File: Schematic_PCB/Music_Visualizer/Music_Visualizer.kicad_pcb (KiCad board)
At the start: 2 copper layers, 141.5 x 82 mm, 232 parts, among them J3 Screw_Terminal_01x02, J5 Screw_Terminal_01x02, J6 3.5mm, Q1 DMP2123LQ-7, SW1 SW_Slide_DPDT, SW2 SW_SPST, U1 LM324, U10 LM3915N-1, U12 LM3915N-1, U13 LM3915N-1, U14 LM3915N-1, U15 LM3915N-1, U16 LM3915N-1, U3 LM324, U4 LM324, U5 LM324, U6 LM324, U7 LM324, U8 LM324

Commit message: pre RDC
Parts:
- removed TP10: T_pw, Custom_Footprints:TEST1Y
- removed TP11: T_mid, Custom_Footprints:TEST1Y
- removed TP12: T_ref, Custom_Footprints:TEST1Y
- removed TP13: T_grnd, Custom_Footprints:TEST1Y
- removed TP14: T_a_out, Custom_Footprints:TEST1Y
- removed TP8: T_a_in, Custom_Footprints:TEST1Y
- removed TP9: T_sig, Custom_Footprints:TEST1Y
- added C11: 100n, Custom_Footprints:custom_C_0805_2012Metric_Pad1.18x1.45mm_HandSolder, B.Cu at (35.5, 48.6)
- added C12: 100n, Custom_Footprints:custom_C_0805_2012Metric_Pad1.18x1.45mm_HandSolder, B.Cu at (35.5, 46.5)
- added C13: 100n, Custom_Footprints:custom_C_0805_2012Metric_Pad1.18x1.45mm_HandSolder, B.Cu at (34.8, 41.0)
- added C14: 100n, Custom_Footprints:custom_C_0805_2012Metric_Pad1.18x1.45mm_HandSolder, B.Cu at (34.8, 43.0)
- added C15: 100n, Custom_Footprints:custom_C_0805_2012Metric_Pad1.18x1.45mm_HandSolder, B.Cu at (27.0, 41.3)
- added C16: 100n, Custom_Footprints:custom_C_0805_2012Metric_Pad1.18x1.45mm_HandSolder, B.Cu at (27.0, 44.2)
- added C17: 10u, Custom_Footprints:custom_C_0805_2012Metric_Pad1.18x1.45mm_HandSolder, F.Cu at (26.2, 40.3)
- added C60: 100n, Custom_Footprints:custom_C_0805_2012Metric_Pad1.18x1.45mm_HandSolder, B.Cu at (30.7, 47.2)
- added D11: LED, PCM_SparkFun-LED:LED_1206_3216Metric_Green, F.Cu at (30.7, 37.1)
- added D12: LED, PCM_SparkFun-LED:LED_1206_3216Metric_Green, F.Cu at (30.7, 34.8)
- added D13: LED, PCM_SparkFun-LED:LED_1206_3216Metric_Green, F.Cu at (30.8, 32.5)
- added D14: LED, PCM_SparkFun-LED:LED_1206_3216Metric_Green, F.Cu at (30.7, 30.3)
- added D15: LED, PCM_SparkFun-LED:LED_1206_3216Metric_Green, F.Cu at (30.8, 28.0)
- added D16: LED, PCM_SparkFun-LED:LED_1206_3216Metric_Green, F.Cu at (30.8, 25.8)
- added D17: LED, PCM_SparkFun-LED:LED_1206_3216Metric_Green, F.Cu at (30.8, 23.5)
- added D18: LED, PCM_SparkFun-LED:LED_1206_3216Metric_Yellow, F.Cu at (30.8, 21.3)
- added D19: LED, PCM_SparkFun-LED:LED_1206_3216Metric_Yellow, F.Cu at (30.8, 19.0)
- added D20: LED, PCM_SparkFun-LED:LED_1206_3216Metric_Red, F.Cu at (30.8, 16.8)
- added R13: 27k, Custom_Footprints:R_0805_2012Metric_Pad1.20x1.40mm_HandSolder, F.Cu at (36.0, 47.6)
- added R14: 6.8k, Custom_Footprints:R_0805_2012Metric_Pad1.20x1.40mm_HandSolder, F.Cu at (30.8, 39.2)
- added R15: 120k, Custom_Footprints:R_0805_2012Metric_Pad1.20x1.40mm_HandSolder, B.Cu at (32.7, 47.3)
- added R16: 12k, Custom_Footprints:R_0805_2012Metric_Pad1.20x1.40mm_HandSolder, F.Cu at (35.2, 39.3)
- added R17: 3.3k, Custom_Footprints:R_0805_2012Metric_Pad1.20x1.40mm_HandSolder, F.Cu at (36.0, 43.5)
- added R18: 56k, Custom_Footprints:R_0805_2012Metric_Pad1.20x1.40mm_HandSolder, B.Cu at (32.0, 42.0)
- added R19: 18k, Custom_Footprints:R_0805_2012Metric_Pad1.20x1.40mm_HandSolder, B.Cu at (29.2, 39.3)
- added R20: 15k, Custom_Footprints:R_0805_2012Metric_Pad1.20x1.40mm_HandSolder, B.Cu at (27.0, 47.0)
- added R21: 39k, Custom_Footprints:R_0805_2012Metric_Pad1.20x1.40mm_HandSolder, B.Cu at (30.0, 42.0)
- added R22: 1k, Custom_Footprints:R_0805_2012Metric_Pad1.20x1.40mm_HandSolder, B.Cu at (29.2, 27.6)
- added R76: 680, Custom_Footprints:R_0805_2012Metric_Pad1.20x1.40mm_HandSolder, B.Cu at (29.2, 20.8)
- added TP2: T_B, Custom_Footprints:NEW_2_TestPoint_Loop_D2.60mm_Drill0.9mm_Beaded, B.Cu at (30.6, 13.8)
- added T_gnd1: T_gnd, Custom_Footprints:NEW_2_TestPoint_Loop_D2.60mm_Drill0.9mm_Beaded, F.Cu at (68.6, 58.8)
- added T_in1: T_in, Custom_Footprints:NEW_2_TestPoint_Loop_D2.60mm_Drill0.9mm_Beaded, F.Cu at (52.6, 52.3)
- added T_mid1: T_mid, Custom_Footprints:NEW_2_TestPoint_Loop_D2.60mm_Drill0.9mm_Beaded, F.Cu at (58.0, 52.8)
- added T_out1: T_out, Custom_Footprints:NEW_2_TestPoint_Loop_D2.60mm_Drill0.9mm_Beaded, F.Cu at (40.3, 52.3)
- added T_pw1: T_pw, Custom_Footprints:NEW_2_TestPoint_Loop_D2.60mm_Drill0.9mm_Beaded, F.Cu at (85.1, 60.6)
- added T_ref1: T_ref, Custom_Footprints:NEW_2_TestPoint_Loop_D2.60mm_Drill0.9mm_Beaded, F.Cu at (35.3, 53.1)
- added T_sig1: T_sig, Custom_Footprints:NEW_2_TestPoint_Loop_D2.60mm_Drill0.9mm_Beaded, F.Cu at (38.1, 52.3)
- added U11: LM3915N-1, Package_DIP:DIP-18_W7.62mm, B.Cu at (27.0, 36.9)
- added U2: LM324, Package_SO:SOIC-14_3.9x8.7mm_P1.27mm, F.Cu at (31.0, 44.8)
- C54, C58, C9, R11, R12: moved to F.Cu
- H1: footprint MountingHole:MountingHole_3.2mm_M3_DIN965 -> Custom_Footprints:Apgriezts_MountingHole_2.2mm_M2
- H2, H3, H4: footprint MountingHole:MountingHole_3.2mm_M3 -> Custom_Footprints:Apgriezts_MountingHole_2.2mm_M2
- J3, J5: footprint TerminalBlock_Phoenix:TerminalBlock_Phoenix_MPT-0,5-2-2.54_1x02_P2.54mm_Horizontal -> Connector_JST:JST_EH_B2B-EH-A_1x02_P2.50mm_Vertical
- J6: footprint PCM_SparkFun-Connector:ScrewTerminal_1x03_P3.5mm_Horizontal_Black -> Connector_JST:JST_EH_B2B-EH-A_1x02_P2.50mm_Vertical
- Q1: moved to B.Cu
- TP1, TP3, TP4, TP5, TP6, TP7: footprint Custom_Footprints:TEST1Y -> Custom_Footprints:NEW_2_TestPoint_Loop_D2.60mm_Drill0.9mm_Beaded; moved to B.Cu
- moved H3 134.5 mm to (36.1, 58.1)
- moved H4 112.2 mm to (57.1, 58.1)
- moved C57 99.3 mm to (32.1, 55.9), turned to -90 degrees
- moved C56 92.5 mm to (25.5, 56.1), turned to 0 degrees
- moved RV2 90.7 mm to (25.1, 53.1)
- moved R74 88.0 mm to (29.3, 56.1), turned to 180 degrees
- moved RV1 84.1 mm to (15.3, 53.1), turned to 0 degrees
- moved C54 50.4 mm to (63.2, 54.8), turned to 180 degrees
- moved C58 50.1 mm to (88.7, 58.8)
- moved R82 49.0 mm to (88.9, 53.3), turned to 90 degrees
- moved SW1 48.8 mm to (48.5, 54.0), turned to -90 degrees
- moved SW2 48.2 mm to (95.2, 53.2), turned to 0 degrees
- moved D71 48.1 mm to (86.8, 53.3), turned to 90 degrees
- moved Q1 45.2 mm to (87.8, 53.6), turned to -90 degrees
- moved J6 42.9 mm to (96.5, 56.1)
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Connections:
- J6 pad 1: Net-(J6-Pin_1) -> GND
- J6 pad 2: GND -> Net-(J6-+)
- Q1 pad 1: Net-(J6-Pin_1) -> Net-(J6-+)
- RV1 pad 1: GND -> unconnected-(RV1-Pad1)
- RV1 pad 3: unconnected-(RV1-Pad3) -> GND
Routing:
- net LED_Brightness_Control: track 292.2 -> 136.3 mm
- net VCC4_5: track 210.8 -> 320.3 mm, vias 7 -> 9
- net +9V: track 300.3 -> 408.0 mm, vias 7 -> 9
- net Vsig: track 56.8 -> 128.4 mm, vias 0 -> 2
- net Net-(C8-Pad2): track 0.00 -> 49.1 mm, vias 0 -> 1
- net Rhi_Value: track 182.1 -> 141.6 mm
- net VBass: track 0.00 -> 33.3 mm, vias 0 -> 1
- net Net-(U8D-+): track 0.00 -> 25.5 mm, vias 0 -> 1
- net Net-(C9-Pad1): track 0.00 -> 15.2 mm
- net Net-(C11-Pad1): track 0.00 -> 14.7 mm, vias 0 -> 2
- net Net-(Q1-S): track 0.00 -> 14.4 mm
- net Net-(J6-+): track 0.00 -> 13.4 mm
- net Net-(C11-Pad2): track 0.00 -> 12.0 mm, vias 0 -> 2
- net Right jack: track 0.00 -> 11.3 mm
- net Net-(U8B-+): track 0.00 -> 10.5 mm
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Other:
- board size 141.5 x 82 mm -> 88.2 x 50.2 mm
- board text added: "+9v"
- board text added: "-24-"
- board text added: "-45-"
- board text added: "-46-"
- board text added: "<IN OUT>"
- board text added: "<OUT IN>"
- board text added: "Brightness"
- board text added: "Mode"
- board text added: "ON OFF"
- board text added: "Sensitivity"
- board text removed: "Bass[60Hz:150Hz]"
- board text removed: "Brilliance[6kHz:20kHz]"
- board text removed: "LED Brightness"
- board text removed: "Low Midrange[150Hz:400Hz]"
- board text removed: "Midrange[400Hz:1kHz]"
- board text removed: "Presence[2.5kHz:6kHz]"
- board text removed: "Upper-Midrange[1kHz:2.5kHz]"
- board text removed: "Volume Range"

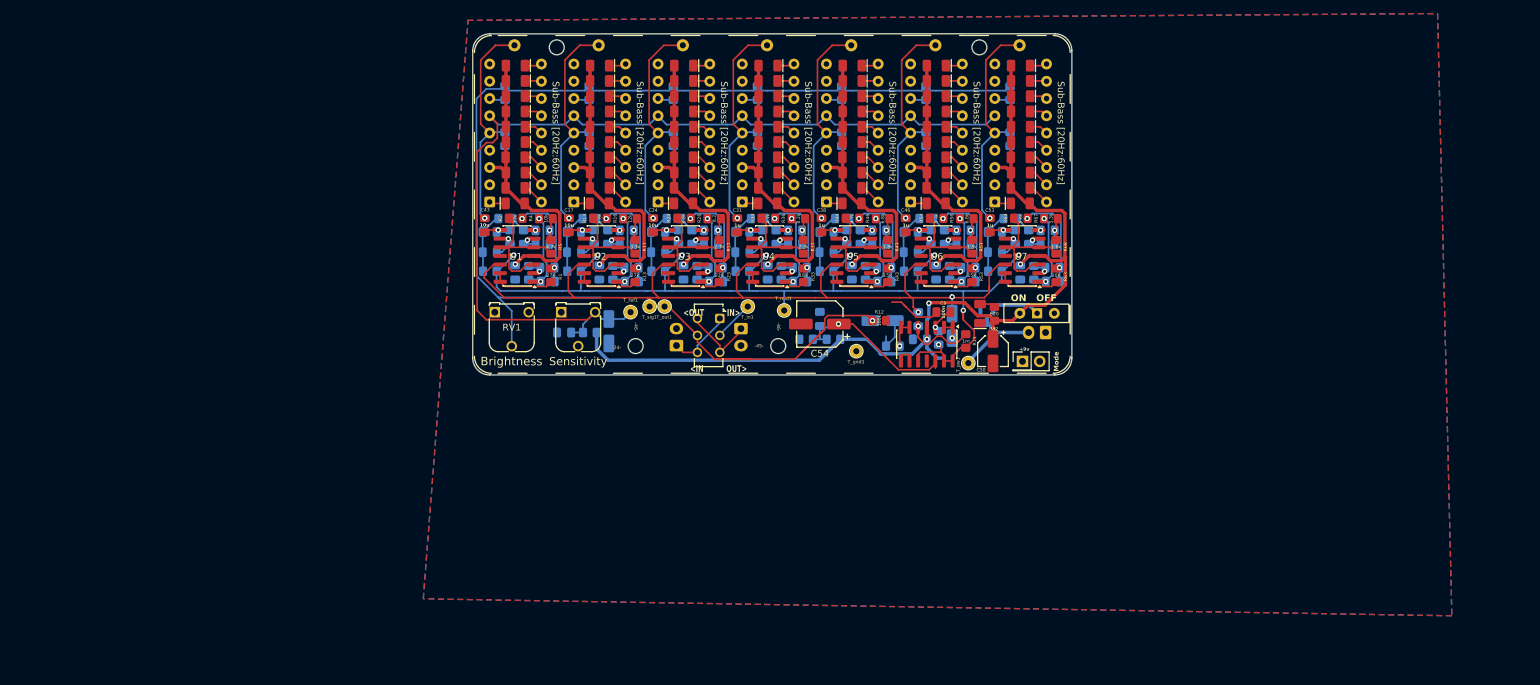
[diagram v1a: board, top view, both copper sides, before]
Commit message: Fixed DRC erros
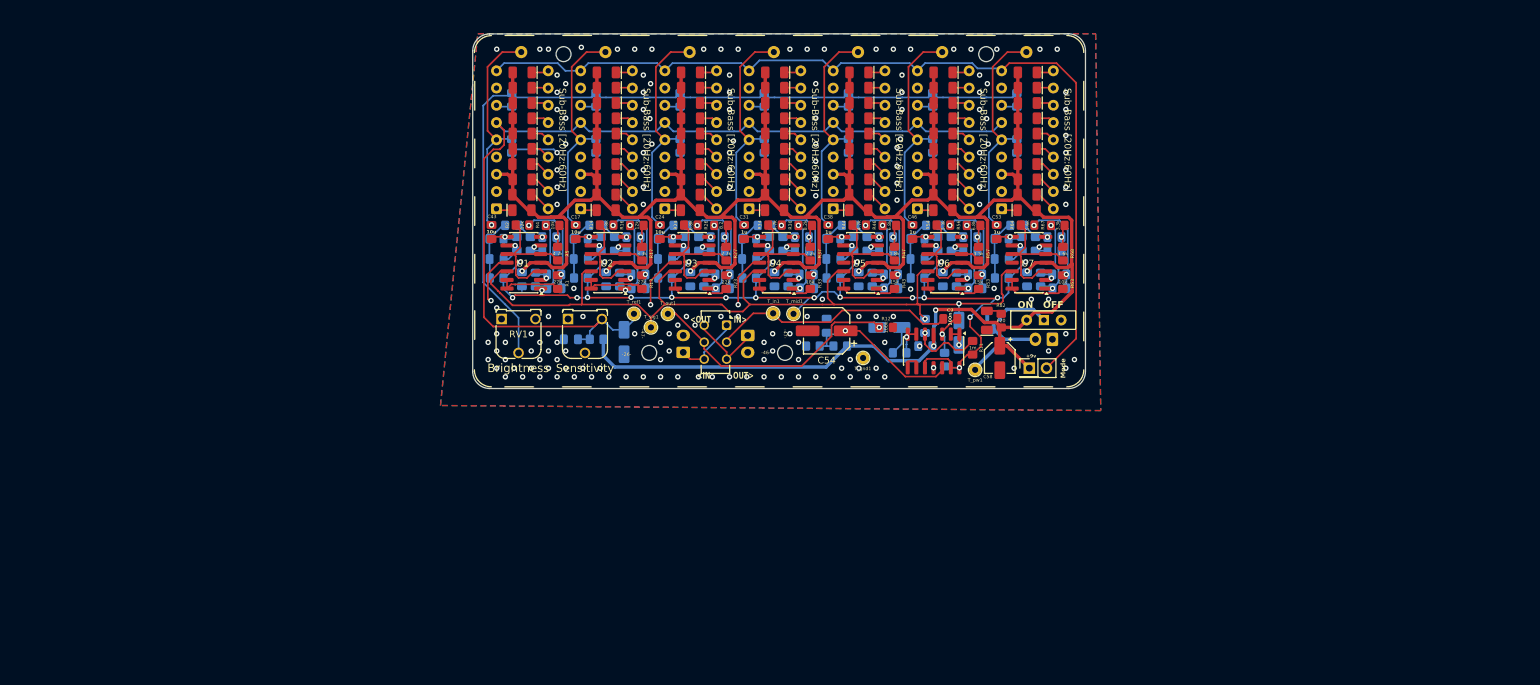
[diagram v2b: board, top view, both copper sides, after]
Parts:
- moved T_in1 3.87 mm to (56.3, 53.3)
- moved R10 3.34 mm to (81.6, 60.1)
- moved T_sig1 3.08 mm to (38.3, 55.3), turned to 180 degrees
- moved C57 2.76 mm to (34.4, 57.5)
- moved H3 2.24 mm to (38.1, 59.1)
- moved T_mid1 1.46 mm to (59.3, 53.3), turned to 180 degrees
- moved C1 1.41 mm to (24.1, 49.6)
- moved C10 1.41 mm to (83.7, 56.1)
- moved C11 1.41 mm to (36.5, 49.6)
- moved C12 1.41 mm to (36.5, 47.5)
- moved C13 1.41 mm to (35.8, 42.0)
- moved C14 1.41 mm to (35.8, 44.0)
- moved C15 1.41 mm to (28.0, 42.3)
- moved C16 1.41 mm to (28.0, 45.2)
- moved C17 1.41 mm to (27.2, 41.3)
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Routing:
- net Mode: track 0.00 -> 136.8 mm
- net +9V: track 408.0 -> 455.6 mm
- net GND: track 0.20 -> 32.4 mm, vias 0 -> 169
- net Net-(C9-Pad1): track 15.2 -> 36.1 mm
- net LED_Brightness_Control: track 136.3 -> 121.1 mm
- net Net-(C8-Pad2): track 49.1 -> 39.0 mm
- net Net-(Q1-S): track 14.4 -> 7.51 mm
- net VCC4_5: track 320.3 -> 315.7 mm, vias 9 -> 21
- net Net-(U8A-+): track 3.60 -> 6.51 mm
- net Rhi_Value: track 141.6 -> 143.2 mm
- net Net-(C8-Pad1): track 5.73 -> 4.28 mm
- net Net-(U8D-+): track 25.5 -> 24.5 mm
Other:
- board size 88.2 x 50.2 mm -> 90.2 x 52.2 mm
- board text added: "-26-"
- board text added: "-47-"
- board text removed: "-24-"
- board text removed: "-45-"
